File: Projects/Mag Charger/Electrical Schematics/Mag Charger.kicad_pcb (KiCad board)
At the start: 2 copper layers, 26 x 27.2 mm, 12 parts, among them J1 Conn_01x08, P1 USB_C_Plug_USB2.0

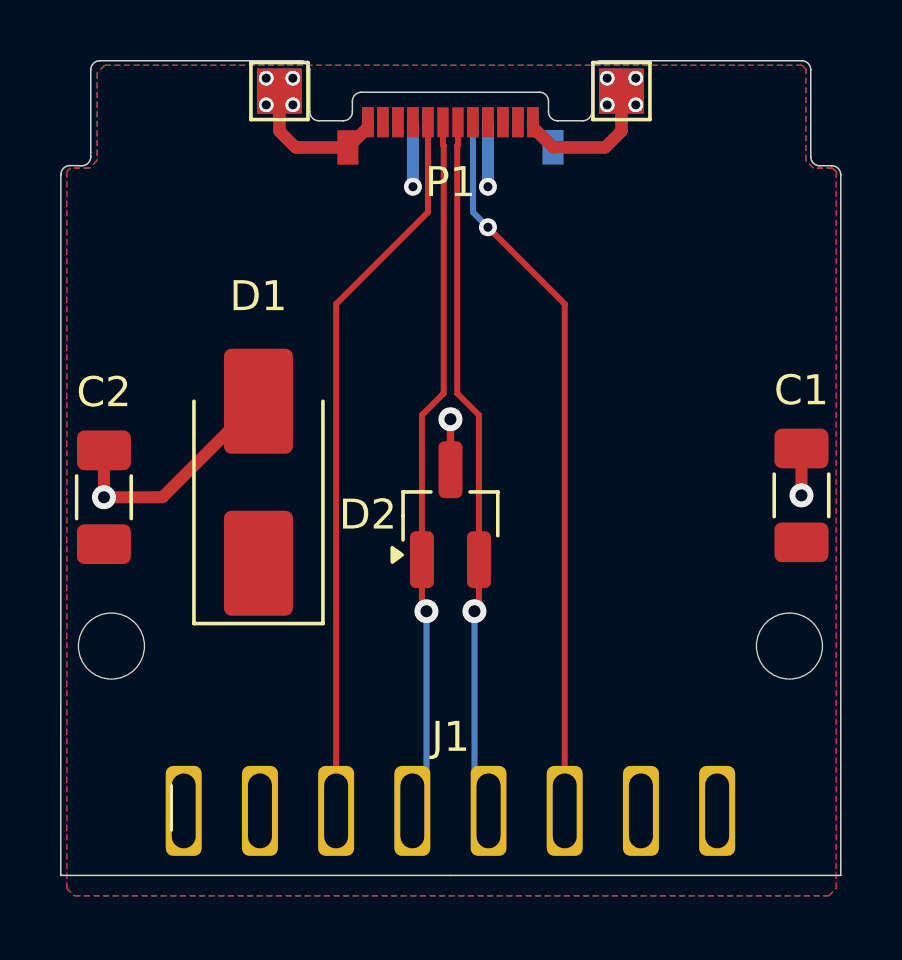
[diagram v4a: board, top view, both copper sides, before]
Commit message: Updated mag charger design
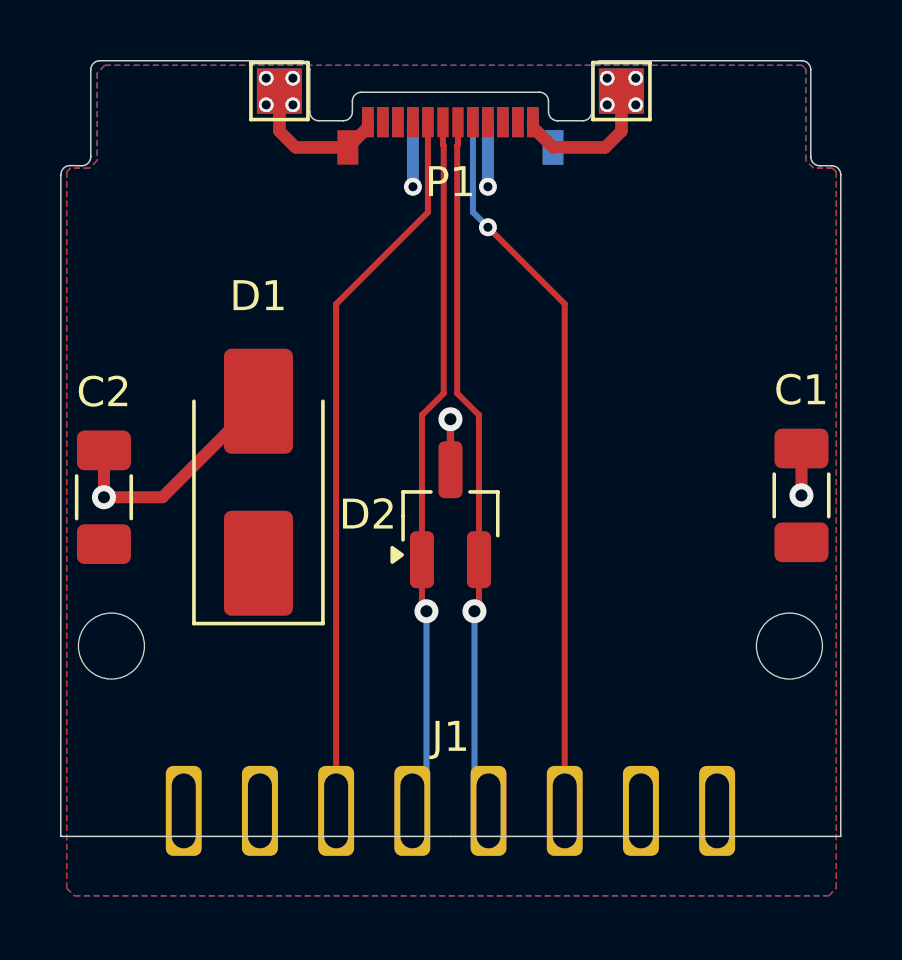
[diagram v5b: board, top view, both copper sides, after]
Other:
- board size 26 x 27.2 mm -> 26 x 25.9 mm
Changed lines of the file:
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@@
 		(embedded_fonts no)
 		(model "${KIPRJMOD}/Custom Parts/1054440001.stp"
+			(hide yes)
 			(offset
 				(xyz 0 3.4 -0.4)
@@
 		(attr through_hole)
 		(fp_line
-			(start -9.3 -0.85)
-			(end -9.3 0.65)
-			(stroke
-				(width 0.1)
+			(start 0 0.85)
+			(end -12.99 0.85)
+			(stroke
+				(width 0.05)
 				(type default)
 			)
-			(layer "F.SilkS")
-		)
-		(fp_line
-			(start 0 2.15)
-			(end -12.99 2.15)
-			(stroke
-				(width 0.05)
-				(type default)
-			)
 			(layer "Edge.Cuts")
 		)
 		(fp_line
-			(start 0 2.15)
-			(end 13.01 2.15)
+			(start 0 0.85)
+			(end 13.01 0.85)
 			(stroke
 				(width 0.05)
@@
 			(size 1.2 3)
 			(drill oval 0.8 2.5)
+			(property pad_prop_castellated)
 			(layers "*.Cu" "*.Mask")
 			(remove_unused_layers no)
@@
 			(size 1.2 3)
 			(drill oval 0.8 2.5)
+			(property pad_prop_castellated)
 			(layers "*.Cu" "*.Mask")
 			(remove_unused_layers no)
@@
 			(size 1.2 3)
 			(drill oval 0.8 2.5)
+			(property pad_prop_castellated)
 			(layers "*.Cu" "*.Mask")
 			(remove_unused_layers no)
@@
 			(size 1.2 3)
 			(drill oval 0.8 2.5)
+			(property pad_prop_castellated)
 			(layers "*.Cu" "*.Mask")
 			(remove_unused_layers no)
@@
 			(size 1.2 3)
 			(drill oval 0.8 2.5)
+			(property pad_prop_castellated)
 			(layers "*.Cu" "*.Mask")
 			(remove_unused_layers no)
@@
 			(size 1.2 3)
 			(drill oval 0.8 2.5)
+			(property pad_prop_castellated)
 			(layers "*.Cu" "*.Mask")
 			(remove_unused_layers no)
@@
 			(size 1.2 3)
 			(drill oval 0.8 2.5)
+			(property pad_prop_castellated)
 			(layers "*.Cu" "*.Mask")
 			(remove_unused_layers no)
@@
 			(size 1.2 3)
 			(drill oval 0.8 2.5)
+			(property pad_prop_castellated)
 			(layers "*.Cu" "*.Mask")
 			(remove_unused_layers no)
@@
 	)
 	(gr_line
-		(start 121.31 150.105)
+		(start 121.31 148.805)
 		(end 121.31105 126.75)
 		(stroke
@@
 	(gr_line
 		(start 95.31585 126.7452)
-		(end 95.31 150.105)
+		(end 95.310326 148.805)
 		(stroke
 			(width 0.05)

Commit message: Fixed for manufacturing
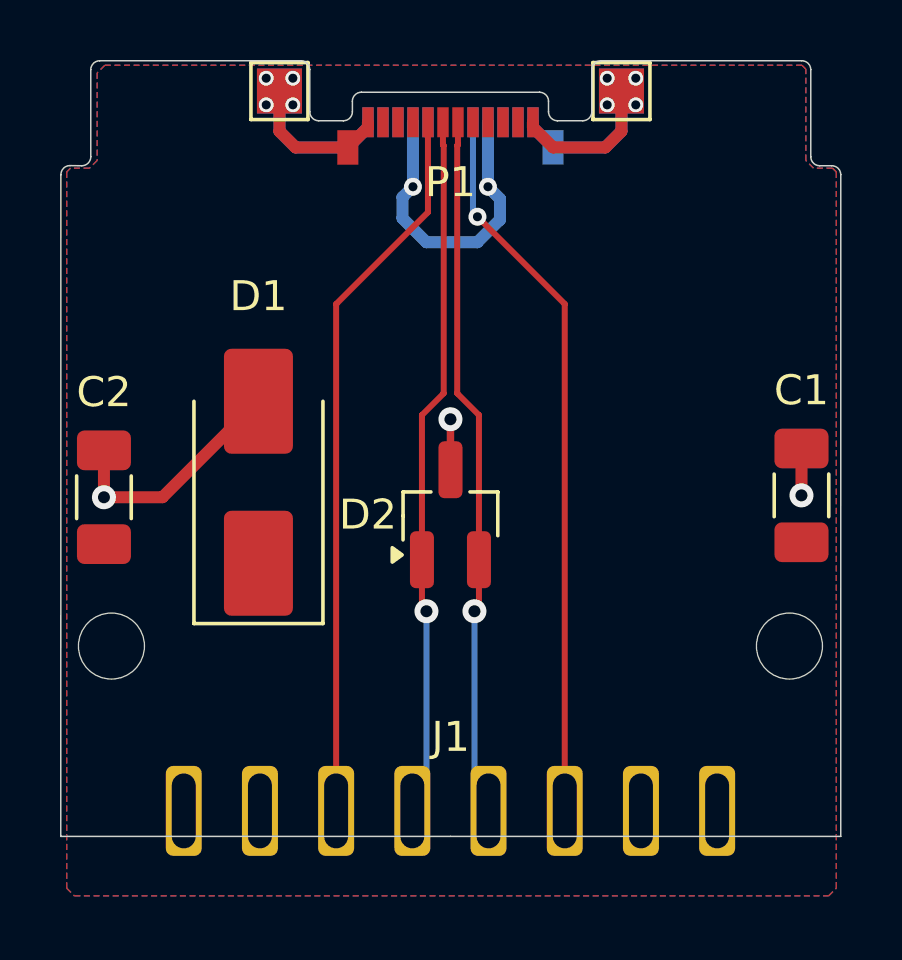
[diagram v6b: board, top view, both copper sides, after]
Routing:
- net VBUS: track 4.86 -> 11.2 mm
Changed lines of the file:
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@@
 		(tenting front back)
 		(pcbplotparams
-			(layerselection 0x00000000_00000000_55555555_57555550)
+			(layerselection 0x00000000_00000000_55555555_5f5555ff)
 			(plot_on_all_layers_selection 0x00000000_00000000_00000000_00000000)
 			(disableapertmacros no)
@@
 			(crossoutdnponfab yes)
 			(subtractmaskfromsilk no)
-			(outputformat 3)
+			(outputformat 1)
 			(mirror no)
 			(drillshape 0)
 			(scaleselection 1)
-			(outputdirectory "")
+			(outputdirectory "../Card Gerbers/")
 		)
 	)
@@
 	)
 	(segment
+		(start 107.5 129)
+		(end 109.199943 129)
+		(width 0.4)
+		(layer "B.Cu")
+		(net 3)
+	)
+	(segment
 		(start 109.55 127.15)
 		(end 109.55 125)
@@
 	)
 	(segment
+		(start 107.05 127.15)
+		(end 106.7 127.5)
+		(width 0.4)
+		(layer "B.Cu")
+		(net 3)
+	)
+	(segment
+		(start 109.95 127.55)
+		(end 109.55 127.15)
+		(width 0.4)
+		(layer "B.Cu")
+		(net 3)
+	)
+	(segment
 		(start 107.05 125)
 		(end 107.05 127.15)
+		(width 0.4)
+		(layer "B.Cu")
+		(net 3)
+	)
+	(segment
+		(start 109.95 128.249943)
+		(end 109.95 127.55)
+		(width 0.4)
+		(layer "B.Cu")
+		(net 3)
+	)
+	(segment
+		(start 106.7 128.2)
+		(end 107.5 129)
+		(width 0.4)
+		(layer "B.Cu")
+		(net 3)
+	)
+	(segment
+		(start 106.7 127.5)
+		(end 106.7 128.2)
+		(width 0.4)
+		(layer "B.Cu")
+		(net 3)
+	)
+	(segment
+		(start 109.199943 129)
+		(end 109.95 128.249943)
 		(width 0.4)
 		(layer "B.Cu")
@@
 	)
 	(segment
-		(start 109.55 128.5)
-		(end 112.11 131.06)
-		(width 0.2)
-		(layer "F.Cu")
-		(net 6)
-	)
-	(segment
 		(start 112.11 131.06)
 		(end 112.11 147.955)
@@
 		(net 6)
 	)
+	(segment
+		(start 109.2 128.15)
+		(end 112.11 131.06)
+		(width 0.2)
+		(layer "F.Cu")
+		(net 6)
+	)
 	(via
-		(at 109.55 128.5)
+		(at 109.2 128.15)
 		(size 0.6)
 		(drill 0.3)
@@
 	)
 	(segment
-		(start 109.05 125)
+		(start 109.05 128)
+		(end 109.05 125)
+		(width 0.2)
+		(layer "B.Cu")
+		(net 6)
+	)
+	(segment
+		(start 109.2 128.15)
 		(end 109.05 128)
 		(width 0.2)
 		(layer "B.Cu")
-		(net 6)
-	)
-	(segment
-		(start 109.05 128)
-		(end 109.55 128.5)
-		(width 0.2)
-		(layer "B.Cu")
